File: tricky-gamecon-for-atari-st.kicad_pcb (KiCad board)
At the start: 2 copper layers, 14 parts, among them J1 Conn_01x09, SW1 GrayHill_series_78_SPDT_DIP_x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, SW2 SW_SPST, SW3 SW_SPST, SW4 SW_SPST, SW5 SW_SPST, SW6 SW_SPST, SW7 SW_SPST, SW8 SW_SPST, SW9 SW_SPST

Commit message: initial tracing
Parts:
- moved SW8 126.8 mm to (127.1, 118.2)
- moved SW7 120.5 mm to (101.7, 118.2)
- moved SW9 117.1 mm to (114.4, 130.8)
- moved SW1 113.6 mm to (88.9, 133.6)
- moved SW6 102.7 mm to (114.4, 105.5)
- moved J1 93.9 mm to (88.9, 105.4)
- moved SW2 93.4 mm to (50.9, 105.5)
- moved D1 90.4 mm to (88.9, 116.8)
- moved D2 89.4 mm to (88.9, 119.4)
- moved SW3 88.7 mm to (38.1, 118.1)
- moved D3 88.3 mm to (88.9, 121.9)
- moved D4 87.3 mm to (88.9, 124.5)
- moved SW4 86.2 mm to (63.5, 118.1)
- moved SW5 79.4 mm to (51.0, 130.8)
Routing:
- net /up: track 0.00 -> 100.0 mm, vias 0 -> 2
- net /down: track 0.00 -> 79.5 mm, vias 0 -> 2
- net /right: track 0.00 -> 64.2 mm, vias 0 -> 2
- net /left: track 0.00 -> 61.6 mm, vias 0 -> 2
- net /fire/lmb: track 0.00 -> 48.2 mm
- net /special_1: track 0.00 -> 40.4 mm
- net Net-(D1-K): track 0.00 -> 37.5 mm
- net /special_2: track 0.00 -> 26.6 mm
- net Net-(D3-K): track 0.00 -> 26.4 mm
- net Net-(SW1-Pad2): track 0.00 -> 5.08 mm
- added copper zone on B.Cu, net GND
- added copper zone on F.Cu, net GND
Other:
- board outline added: 109.2 x 45.7 mm

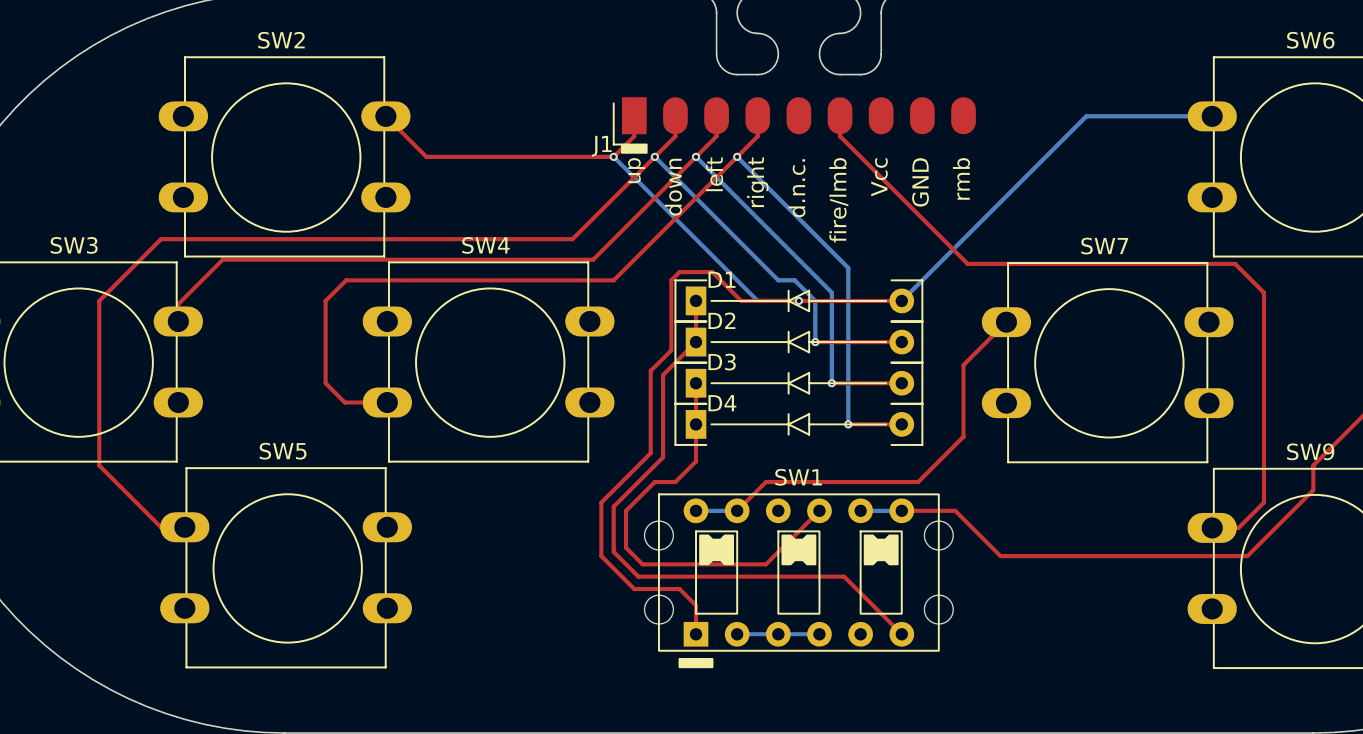
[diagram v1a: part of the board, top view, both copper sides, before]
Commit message: update pcb, add mounting holes
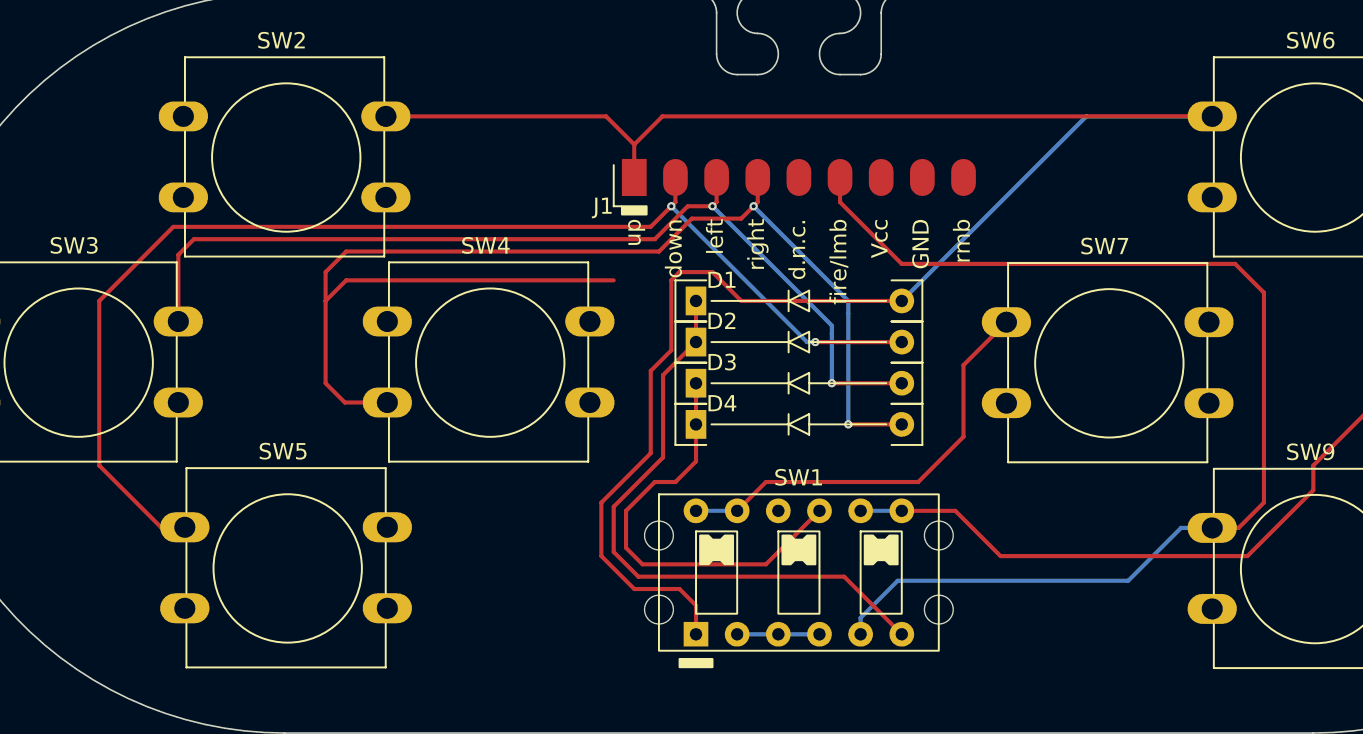
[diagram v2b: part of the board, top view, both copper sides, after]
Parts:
- moved J1 3.81 mm to (88.9, 109.2)
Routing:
- net /fire/lmb: track 48.2 -> 71.8 mm
- net /up: track 100.0 -> 121.2 mm, vias 2 -> 0
- net /right: track 64.2 -> 78.6 mm
- net /down: track 79.5 -> 74.3 mm
- net /left: track 61.6 -> 58.5 mm

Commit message: Prepare release : v1.0.0-RC1
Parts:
- added G***: LOGO, cliparts:logo--cc--cc, F.Cu at (74.4, 100.8)
- added G***: LOGO, cliparts:logo--cc--zero, F.Cu at (79.0, 100.8)
- added H1: M2.5, MountingHole:MountingHole_2.7mm_M2.5, F.Cu at (40.0, 111.1)
- added H2: M2.5, MountingHole:MountingHole_2.7mm_M2.5, F.Cu at (40.0, 130.2)
- added H3: M2.5, MountingHole:MountingHole_2.7mm_M2.5, F.Cu at (68.6, 101.0)
- added H4: M2.5, MountingHole:MountingHole_2.7mm_M2.5, F.Cu at (68.6, 140.3)
- added H5: M2.5, MountingHole:MountingHole_2.7mm_M2.5, F.Cu at (109.2, 101.0)
- added H6: M2.5, MountingHole:MountingHole_2.7mm_M2.5, F.Cu at (109.2, 140.3)
- added H7: M2.5, MountingHole:MountingHole_2.7mm_M2.5, F.Cu at (137.8, 111.1)
- added H8: M2.5, MountingHole:MountingHole_2.7mm_M2.5, F.Cu at (137.8, 130.2)
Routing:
- net /rmb: track 0.00 -> 26.5 mm, vias 0 -> 1
- net /up: track 121.2 -> 146.2 mm
- net /special_1: track 40.4 -> 64.5 mm
- net /left: track 58.5 -> 71.0 mm
- net /special_2: track 26.6 -> 39.1 mm
- net /fire/lmb: track 71.8 -> 84.3 mm
- net /down: track 74.3 -> 86.8 mm
- net /right: track 78.6 -> 72.8 mm
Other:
- board text added: "Tricky gamecon for the Atari ST family v1.0.0-RC1"
- board text added: "WITHOUT ANY WARRANTY Without even the implied warranty of SAFETY, MERCHANTABILITY or FITNESS FOR A PARTICULAR PURPOSE"
- board text added: "https://github.com/sporniket/tricky-gamecon-for-atari-st"
